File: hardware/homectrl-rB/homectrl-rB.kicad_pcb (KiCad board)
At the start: 4 copper layers, 134 x 84.3 mm, 122 parts, among them J1 Barrel_Jack, J2 USB_C_Female_USB2_Small, J3 SMS-CONN-0, J4 SMS-CONN-1, J5 ALS_CONN, J6 PUMP0-CONN, J7 PUMP1-CONN, J8 STEP-CONN, Q1 DMP6023LE-13, Q2 AO3400A, Q3 AO3400A, SW1 SW_RESET, SW2 SW_BOOT, U1 ESP32-S3-WROOM-1, U2 TPS5405DR, U3 ID_LM66100DCKR, U4 ID_LM66100DCKR, U5 ADS1115IDGS, U6 SI2301, U7 SI2301, U8 TMC2209

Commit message: swap connector in progress
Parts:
- removed D10, D11: SMAJ5.0A, Diode_SMD:D_SMA
- added C14: 0.1uF, Capacitor_SMD:C_0603_1608Metric, F.Cu at (89.0, 83.6)
- added U9: TPD2E001DRLR, TPD2E001DRLR:SOT50P160X60-5N, F.Cu at (89.2, 85.8)
- C1, C41: value 100uF 35V -> 100uF
- C10: value 10uF 16V -> 10uF
- C11, C12: value 1uF 12V -> 1uF
- C13, C18, C20: value 0.1uF 25V -> 0.1uF
- C15, C28, C31, C32, C34, C42, C43: value 0.1uF 50V -> 0.1uF
- C16, C25, C26: value 10uF 12V -> 10uF
- C17, C19, C2: value 10uF 25V -> 10uF
- C21, C22, C23, C24, C35, C36: value 0.1uF 12V -> 0.1uF
- C27: value 2.2uF 35V -> 2.2uF
- C29: value 22nF 50V -> 22nF
- C3: value 47 nF 50V -> 47 nF
- C30: value 4.7uF 50V -> 4.7uF
- C33: value 220uF 35V -> 220uF
- C37: value 10uF 50V -> 10uF
- C4: value 3.3nF 16V -> 3.3nF
- C5: value 47nF 25V -> 47nF
- C6: value 47uF 16V -> 47uF
- C7: value 0.47uF 16V -> 0.47uF
- C8: value 22uF 16V -> 22uF
- C9: value 47uF 12V -> 47uF
- D1: value SS14 -> SS24
- J3, J4: footprint ul_530480310:CONN03_530480310_MOL -> LIB_S03B-PASK-2_LF__SN_:S03BPASK2LFSN
- J5, J8: footprint 530480410:MOLEX_530480410 -> S04B_PASK_2:CONN4_S04B-PASK_JST
- J6, J7: footprint 530480210:MOLEX_530480210 -> S02B_PASK_2:CONN2_S02B-PASK-2_JST
- moved J3 96.1 mm to (178.4, 114.4), turned to 90 degrees
- moved J4 95.3 mm to (178.4, 103.1), turned to 90 degrees
- moved J5 90.1 mm to (174.8, 90.4), turned to 0 degrees
- moved J7 57.1 mm to (211.2, 101.4), turned to -90 degrees
- moved J6 54.2 mm to (211.2, 91.5), turned to -90 degrees
- moved J8 36.9 mm to (179.2, 130.2)
- moved J2 0.07 mm to (138.8, 122.0)
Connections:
- Q1 pad 4: Net-(D2-A1) -> (no net)
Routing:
- net AOUT-0: track 19.3 -> 27.0 mm
- net GND: track 177.0 -> 169.4 mm, vias 328 -> 314
- net +3V3: track 293.6 -> 300.4 mm
- net AOUT-1: track 23.8 -> 26.6 mm
- removed copper zone on In1.Cu, net GND
- removed copper zone on In2.Cu, net GND
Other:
- board size 134 x 84.3 mm -> 134 x 86.1 mm
- board text removed: "+ -"
- board text removed: "- DC PUMP x2 - STEP"
- board text removed: "1A 1B 2A 2B"
- board text removed: ">>>"
- board text removed: "ACT-IN >"
- board text removed: "SMS1"

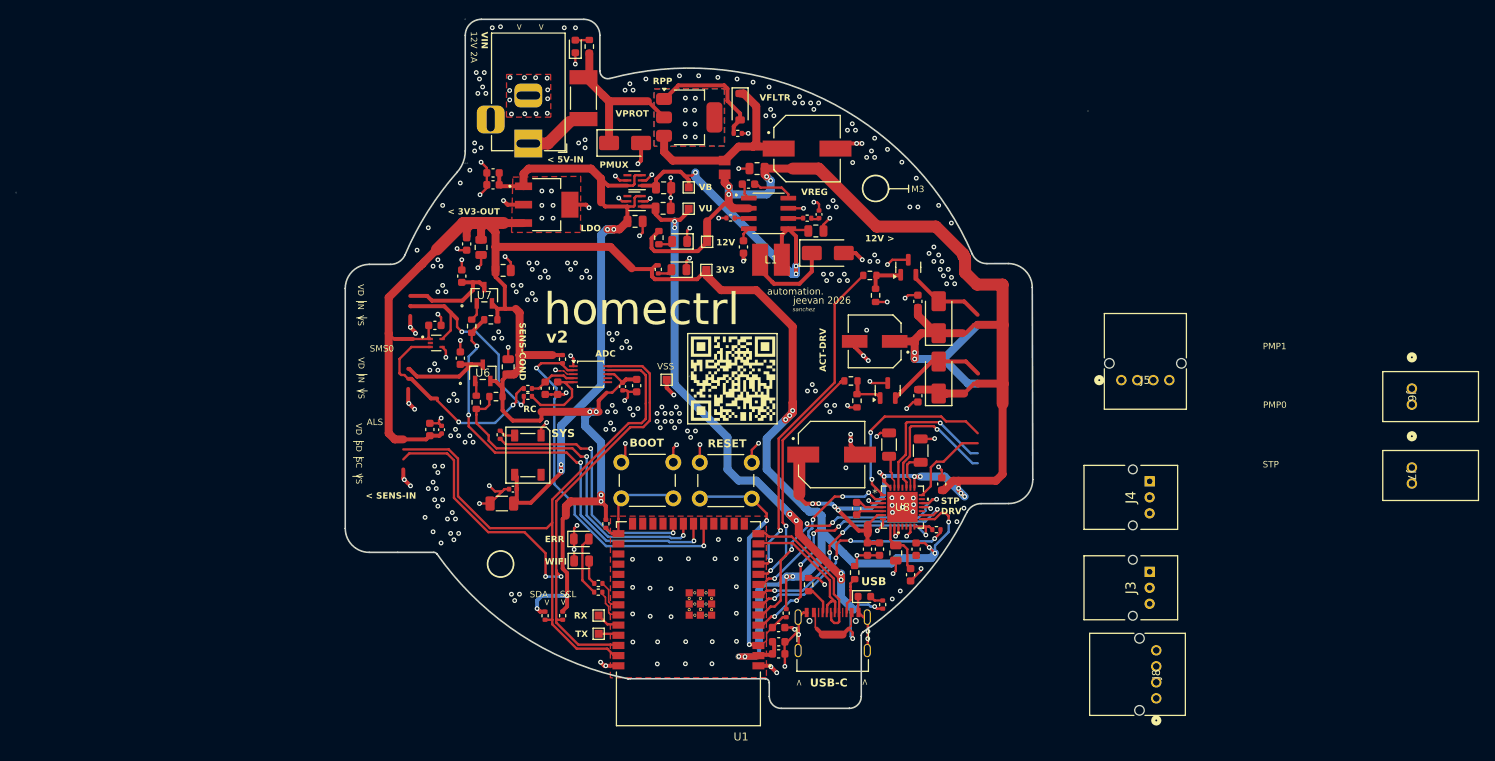
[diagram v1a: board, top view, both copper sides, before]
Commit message: changes for connector revision
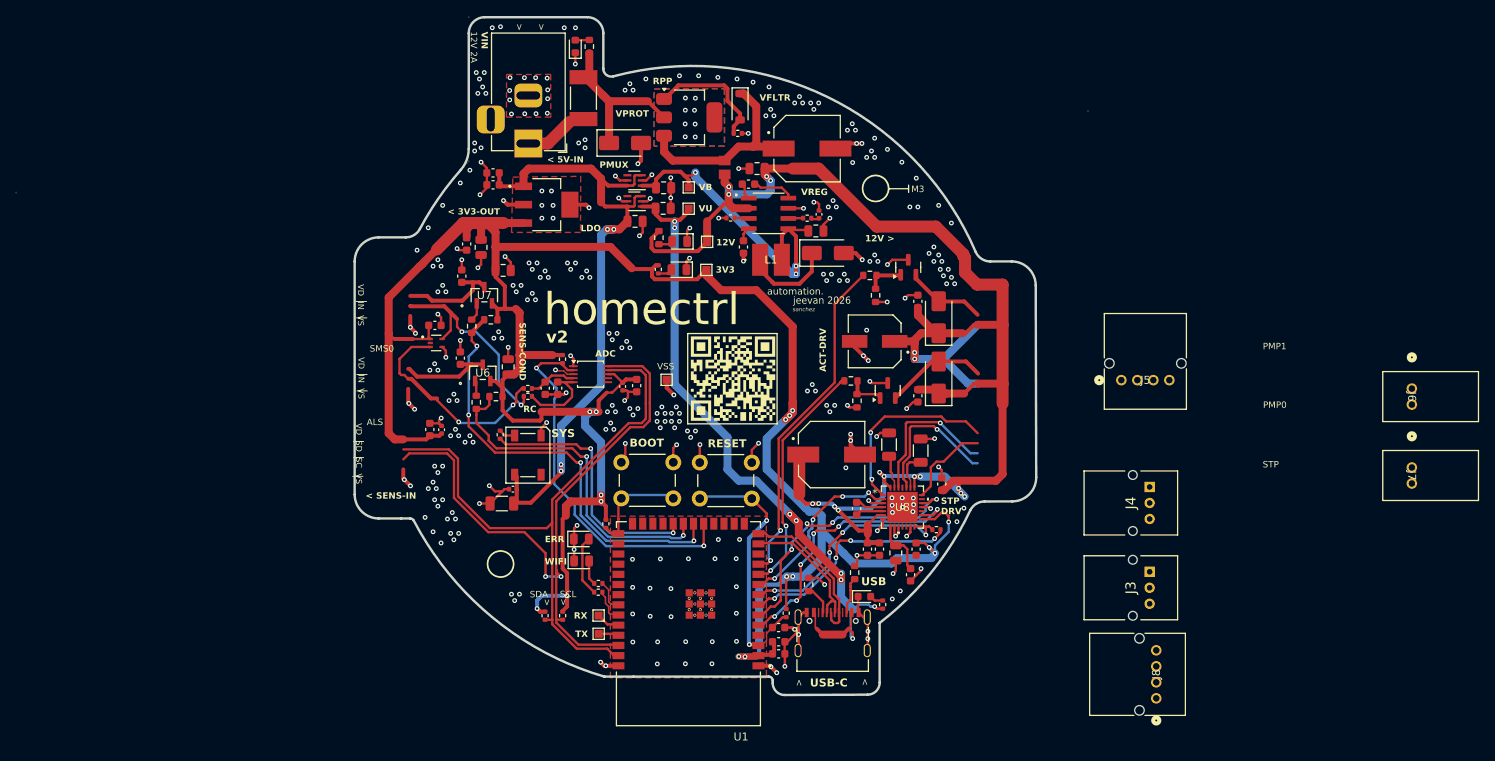
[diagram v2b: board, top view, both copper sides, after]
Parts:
- moved J4 0.70 mm to (178.4, 103.8)
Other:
- board size 134 x 86.1 mm -> 134 x 84.7 mm

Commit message: connector fixes
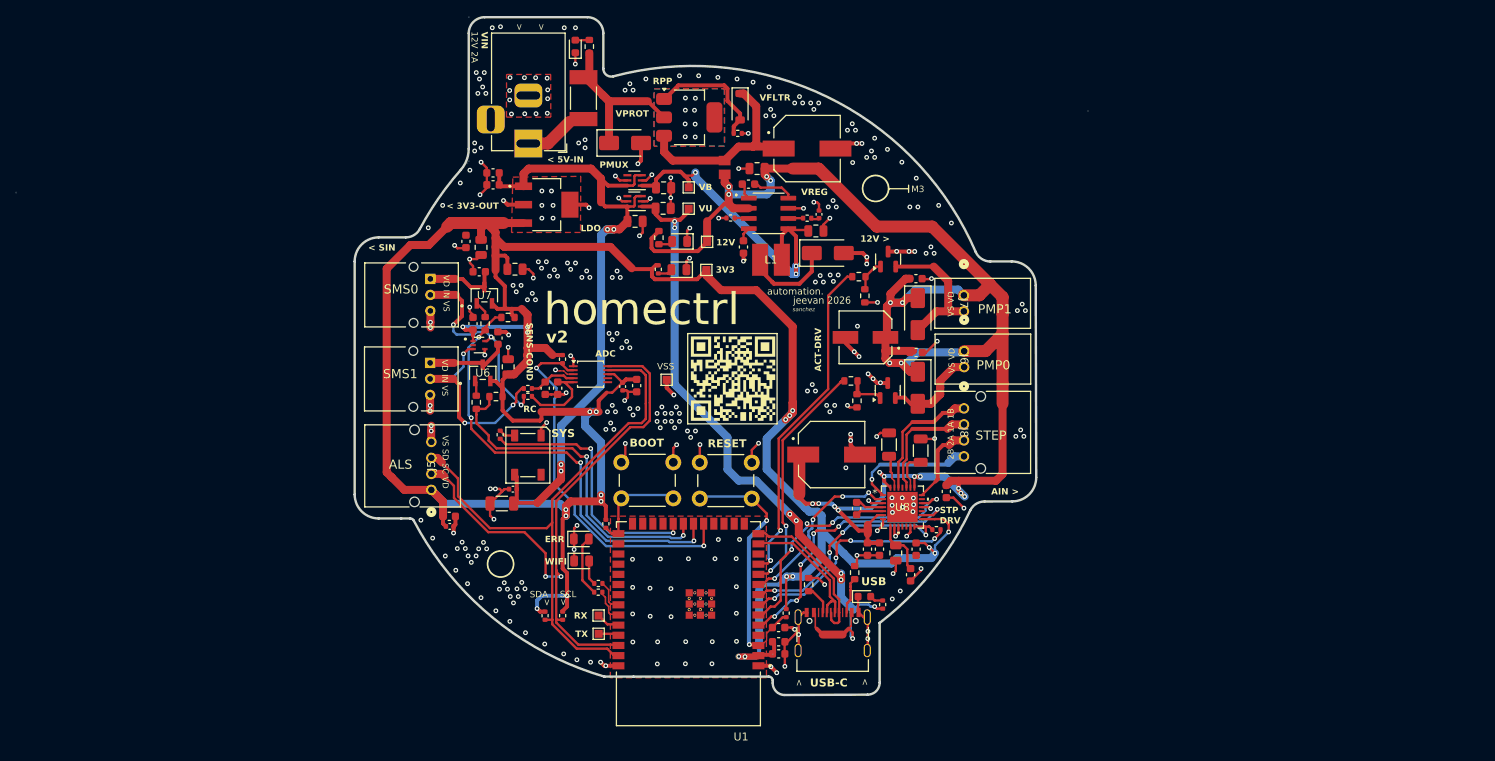
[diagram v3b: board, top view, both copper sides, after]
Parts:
- moved J3 93.7 mm to (88.4, 88.3)
- moved J4 93.6 mm to (88.5, 77.8)
- moved J5 87.3 mm to (88.6, 104.2), turned to 90 degrees
- moved J7 60.0 mm to (155.2, 79.8)
- moved J6 56.2 mm to (155.2, 86.8)
- moved J8 43.5 mm to (155.2, 94.0), turned to -90 degrees
- moved C18 12.1 mm to (90.9, 108.7), turned to 0 degrees
- moved C17 11.1 mm to (90.8, 107.5), turned to 0 degrees
- moved C43 5.42 mm to (149.2, 87.0), turned to 0 degrees
- moved U9 5.35 mm to (94.5, 86.1)
- moved C23 5.33 mm to (96.9, 85.2)
- moved C14 4.77 mm to (93.8, 83.4), turned to -90 degrees
- moved D12 2.91 mm to (149.4, 91.4), turned to -90 degrees
- moved C42 2.85 mm to (149.2, 77.8), turned to 0 degrees
- moved Q3 2.72 mm to (145.7, 75.3)
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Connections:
- J5 pad 2: S3-SDA -> S3-SCL
- J5 pad 3: S3-SCL -> S3-SDA
- J8 pad 1: 1A -> 1B
- J8 pad 2: 1B -> 1A
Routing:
- net +3V3: track 300.4 -> 336.0 mm, vias 16 -> 21
- net 2B: track 23.7 -> 15.8 mm, vias 2 -> 1
- net PUMP1-N: track 10.1 -> 17.8 mm
- net S3-SCL: track 84.2 -> 77.4 mm
- net S3-SDA: track 78.4 -> 73.0 mm
- net SVDD1: track 12.7 -> 9.12 mm
- net 1A: track 18.5 -> 15.1 mm, vias 1 -> 0
- net 1B: track 19.1 -> 16.1 mm, vias 1 -> 0
- net +12V: track 201.8 -> 204.3 mm, vias 17 -> 19
- net GND: track 169.4 -> 171.6 mm, vias 314 -> 303
- net SVDD0: track 11.8 -> 10.2 mm
- net PUMP0-N: track 13.2 -> 11.8 mm
- net SGATE-1: track 55.0 -> 56.1 mm
- net 2A: track 11.1 -> 10.2 mm
- net Net-(Q3-Pad1): track 4.77 -> 4.01 mm
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- added copper zone on In1.Cu, net GND
- added copper zone on In2.Cu, net GND
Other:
- board text added: "2B 2A 1A 1B"
- board text added: "< SIN"
- board text added: "AIN >"
- board text added: "SMS1"
- board text added: "STEP"
- board text added: "VS SD SC VD"
- board text added: "VS VD"
- board text added: "jeevan sanchez | 2026.01.16"
- board text removed: "- SMS x2 - ALS"
- board text removed: "< SENS-IN"
- board text removed: "STP"
- board text removed: "VD SD SC VS"
- board text removed: "jeevan sanchez | 2026.01.12"
- board text removed: "|"

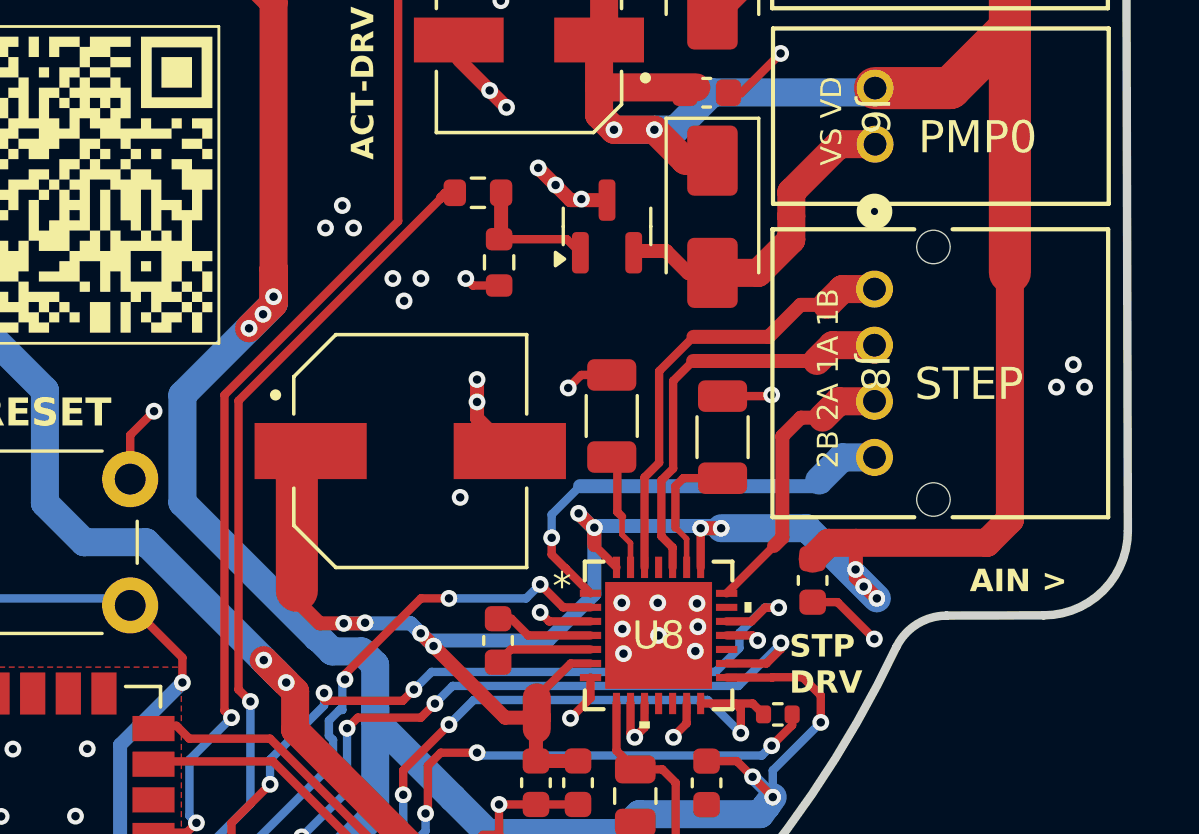
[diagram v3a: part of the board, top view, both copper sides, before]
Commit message: more conn changes
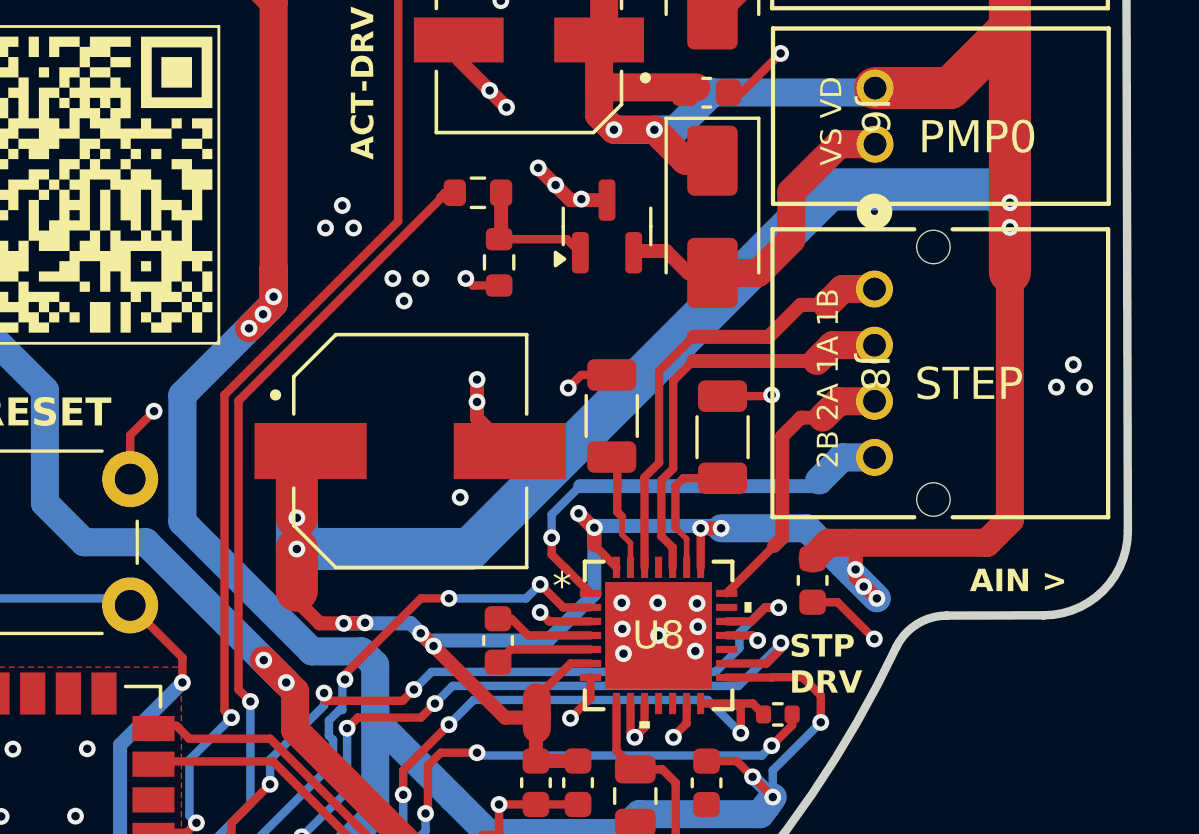
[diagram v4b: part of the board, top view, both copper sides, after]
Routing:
- net +12V: track 204.3 -> 236.0 mm, vias 19 -> 23
- removed copper zone on In1.Cu, net GND
- removed copper zone on In2.Cu, net GND
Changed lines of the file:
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@@
 		(tags "capacitor")
 		(property "Reference" "C18"
-			(at 0 -1.16 360)
+			(at 0 -1.16 0)
 			(layer "F.SilkS")
 			(hide yes)
@@
 		)
 		(fp_text user "${REFERENCE}"
-			(at 0 0 360)
+			(at 0 0 0)
 			(layer "F.Fab")
 			(effects
@@
 		(tags "capacitor")
 		(property "Reference" "C43"
-			(at 0 -1.43 360)
+			(at 0 -1.43 0)
 			(layer "F.SilkS")
 			(hide yes)
@@
 		)
 		(property "Value" "0.1uF"
-			(at -12.4 -0.8 360)
+			(at -12.4 -0.8 0)
 			(layer "F.Fab")
 			(effects
@@
 		)
 		(fp_text user "${REFERENCE}"
-			(at 0 0 360)
+			(at 0 0 0)
 			(layer "F.Fab")
 			(effects
@@
 		(tags "capacitor")
 		(property "Reference" "C42"
-			(at 0 -1.43 360)
+			(at 0 -1.43 0)
 			(layer "F.SilkS")
 			(hide yes)
@@
 		)
 		(property "Value" "0.1uF"
-			(at 0 1.43 360)
+			(at 0 1.43 0)
 			(layer "F.Fab")
 			(effects
@@
 		)
 		(fp_text user "${REFERENCE}"
-			(at 0 0 360)
+			(at 0 0 0)
 			(layer "F.Fab")
 			(effects
@@
 		(tags "capacitor")
 		(property "Reference" "C17"
-			(at 0 -1.43 360)
+			(at 0 -1.43 0)
 			(layer "F.SilkS")
 			(hide yes)
@@
 		)
 		(property "Value" "10uF "
-			(at -0.15 1.18 360)
+			(at -0.15 1.18 0)
 			(layer "F.Fab")
 			(effects
@@
 		)
 		(fp_text user "${REFERENCE}"
-			(at 0 0 360)
+			(at 0 0 0)
 			(layer "F.Fab")
 			(effects
@@
 		(tags "capacitor")
 		(property "Reference" "C24"
-			(at 0 -1.43 360)
+			(at 0 -1.43 0)
 			(layer "F.SilkS")
 			(hide yes)
@@
 		)
 		(property "Value" "0.1uF "
-			(at 0 1.43 360)
+			(at 0 1.43 0)
 			(layer "F.Fab")
 			(effects
@@
 		)
 		(fp_text user "${REFERENCE}"
-			(at 0 0 360)
+			(at 0 0 0)
 			(layer "F.Fab")
 			(effects
@@
 	)
 	(segment
-		(start 134.58 104.73)
-		(end 134.58 100.24)
+		(start 134.58 103.24)
+		(end 134.58 104.73)
 		(width 1.5)
 		(layer "F.Cu")
@@
 	)
 	(segment
-		(start 159.97 90.88)
-		(end 159.99 90.9)
-		(width 1)
-		(layer "F.Cu")
-		(net 1)
-	)
-	(segment
 		(start 145.88 88.3)
 		(end 147.32 88.3)
@@
 	)
 	(segment
+		(start 134.58 102.13)
+		(end 134.58 100.24)
+		(width 1.5)
+		(layer "F.Cu")
+		(net 1)
+	)
+	(segment
 		(start 145.53 82.91)
 		(end 145.53 85.26)
@@
 	)
 	(via
+		(at 134.58 102.13)
+		(size 0.6)
+		(drill 0.3)
+		(layers "F.Cu" "B.Cu")
+		(net 1)
+	)
+	(via
+		(at 134.58 103.24)
+		(size 0.6)
+		(drill 0.3)
+		(layers "F.Cu" "B.Cu")
+		(net 1)
+	)
+	(via
 		(at 154.49 103.97)
 		(size 0.6)
@@
 	)
 	(via
+		(at 159.99 90.9)
+		(size 0.6)
+		(drill 0.3)
+		(layers "F.Cu" "B.Cu")
+		(net 1)
+	)
+	(via
 		(at 139.45 106.7)
 		(size 0.6)
@@
 	)
 	(via
+		(at 159.99 91.78)
+		(size 0.6)
+		(drill 0.3)
+		(layers "F.Cu" "B.Cu")
+		(net 1)
+	)
+	(via
 		(at 136.25 105.89)
 		(size 0.6)
@@
 	)
 	(segment
+		(start 134.58 102.13)
+		(end 134.58 103.24)
+		(width 1.5)
+		(layer "B.Cu")
+		(net 1)
+	)
+	(segment
 		(start 145.18 104.850331)
 		(end 145.18 102.53)
@@
 	)
 	(segment
+		(start 140.733705 103.24)
+		(end 134.58 103.24)
+		(width 1.5)
+		(layer "B.Cu")
+		(net 1)
+	)
+	(segment
 		(start 148.06 88.3)
 		(end 145.88 88.3)
@@
 	)
 	(segment
+		(start 159.99 90.9)
+		(end 159.99 91.78)
+		(width 1.5)
+		(layer "B.Cu")
+		(net 1)
+	)
+	(segment
 		(start 130.519607 67.230393)
 		(end 131 66.75)
@@
 	)
 	(segment
+		(start 159.515301 90.425301)
+		(end 153.548404 90.425301)
+		(width 1.5)
+		(layer "B.Cu")
+		(net 1)
+	)
+	(segment
 		(start 147.47 80.76)
 		(end 145.97 80.76)
@@
 	)
 	(segment
+		(start 159.99 90.9)
+		(end 159.515301 90.425301)
+		(width 1.5)
+		(layer "B.Cu")
+		(net 1)
+	)
+	(segment
 		(start 155.029599 86.97)
 		(end 155.184699 86.8149)
@@
 	)
 	(segment
+		(start 153.548404 90.425301)
+		(end 140.733705 103.24)
+		(width 1.5)
+		(layer "B.Cu")
+		(net 1)
+	)
+	(segment
 		(start 149.7 102.5)
 		(end 152.75 102.5)
@@
 	)
 	(segment
+		(start 136.89 106.89)
+		(end 137.37 107.37)
+		(width 1)
+		(layer "B.Cu")
+		(net 9)
+	)
+	(segment
 		(start 140.137893 112.112107)
 		(end 137.37 109.344214)
@@
 	)
 	(segment
-		(start 135.314214 106.4)
-		(end 135.345786 106.4)
+		(start 130.5 102.27)
+		(end 135.12 106.89)
 		(width 1)
 		(layer "B.Cu")
@@
 	)
 	(segment
-		(start 135.835786 106.89)
-		(end 136.89 106.89)
-		(width 1)
-		(layer "B.Cu")
-		(net 9)
-	)
-	(segment
 		(start 151.304315 112.410309)
 		(end 151.54 112.081598)
@@
 	)
 	(segment
-		(start 136.89 106.89)
-		(end 137.37 107.37)
-		(width 1)
-		(layer "B.Cu")
-		(net 9)
-	)
-	(segment
 		(start 146.107893 113.362107)
 		(end 146.78 112.69)
@@
 	)
 	(segment
+		(start 137.37 107.37)
+		(end 137.37 108.92)
+		(width 1)
+		(layer "B.Cu")
+		(net 9)
+	)
+	(segment
 		(start 109.8 104.8)
 		(end 109.8 105.6)
@@
 	)
 	(segment
-		(start 137.37 107.37)
-		(end 137.37 108.92)
+		(start 130.5 97.75)
+		(end 130.5 102.27)
 		(width 1)
 		(layer "B.Cu")
@@
 	)
 	(segment
-		(start 133.75 94.25)
-		(end 133.75 94.5)
+		(start 133.75 94.5)
+		(end 130.5 97.75)
+		(width 1)
+		(layer "B.Cu")
+		(net 9)
+	)
+	(segment
+		(start 135.12 106.89)
+		(end 136.89 106.89)
 		(width 1)
 		(layer "B.Cu")
@@
 	)
 	(segment
-		(start 130.5 101.585786)
-		(end 135.314214 106.4)
-		(width 1)
-		(layer "B.Cu")
-		(net 9)
-	)
-	(segment
 		(start 101.8 118)
 		(end 101.8 119)
@@
 	)
 	(segment
+		(start 133.75 94.25)
+		(end 133.75 94.5)
+		(width 1)
+		(layer "B.Cu")
+		(net 9)
+	)
+	(segment
 		(start 129.55 116.69)
 		(end 130.24 116)
@@
 	)
 	(segment
-		(start 133.75 94.5)
-		(end 130.5 97.75)
-		(width 1)
-		(layer "B.Cu")
-		(net 9)
-	)
-	(segment
-		(start 130.5 97.75)
-		(end 130.5 101.585786)
-		(width 1)
-		(layer "B.Cu")
-		(net 9)
-	)
-	(segment
 		(start 88.585301 104.163149)
 		(end 90.322152 105.9)
@@
 	)
 	(segment
-		(start 135.345786 106.4)
-		(end 135.835786 106.89)
-		(width 1)
-		(layer "B.Cu")
-		(net 9)
-	)
-	(segment
 		(start 141.387893 113.362107)
 		(end 146.107893 113.362107)
@@
 			)
 		)
-	)
-	(zone
-		(net 2)
-		(net_name "GND")
-		(layers "In1.Cu" "In2.Cu")
-		(name "GND")
-		(hatch edge 0.5)
-		(priority 4)
-		(connect_pads
-			(clearance 0.5)
-		)
-		(min_thickness 0.25)
-		(filled_areas_thickness no)
-		(fill yes
-			(thermal_gap 0.5)
-			(thermal_bridge_width 0.5)
-		)
-		(polygon
-			(pts
-				(xy 77.14 43.82) (xy 166.19 43.82) (xy 166.19 135.46) (xy 77.14 135.46)
-			)
-		)

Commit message: add AGND, more layout work
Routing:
- added copper zone on In1.Cu, net GND
- added copper zone on In2.Cu, net GND
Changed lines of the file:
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@@
+		)
+	)
+	(zone
+		(net 2)
+		(net_name "GND")
+		(layers "In1.Cu" "In2.Cu")
+		(name "GND")
+		(hatch edge 0.5)
+		(priority 4)
+		(connect_pads
+			(clearance 0.5)
+		)
+		(min_thickness 0.25)
+		(filled_areas_thickness no)
+		(fill yes
+			(thermal_gap 0.5)
+			(thermal_bridge_width 0.5)
+		)
+		(polygon
+			(pts
+				(xy 77.4 43.8) (xy 166.2 44) (xy 166 135.4) (xy 77 135.4)
+			)
 		)
 	)
